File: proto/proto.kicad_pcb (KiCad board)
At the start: 4 copper layers, 57.7 x 90 mm, 17 parts, among them J1 J1, J2 J2, J3 J3, J4 J4, J5 J5, U2 TPIC6595

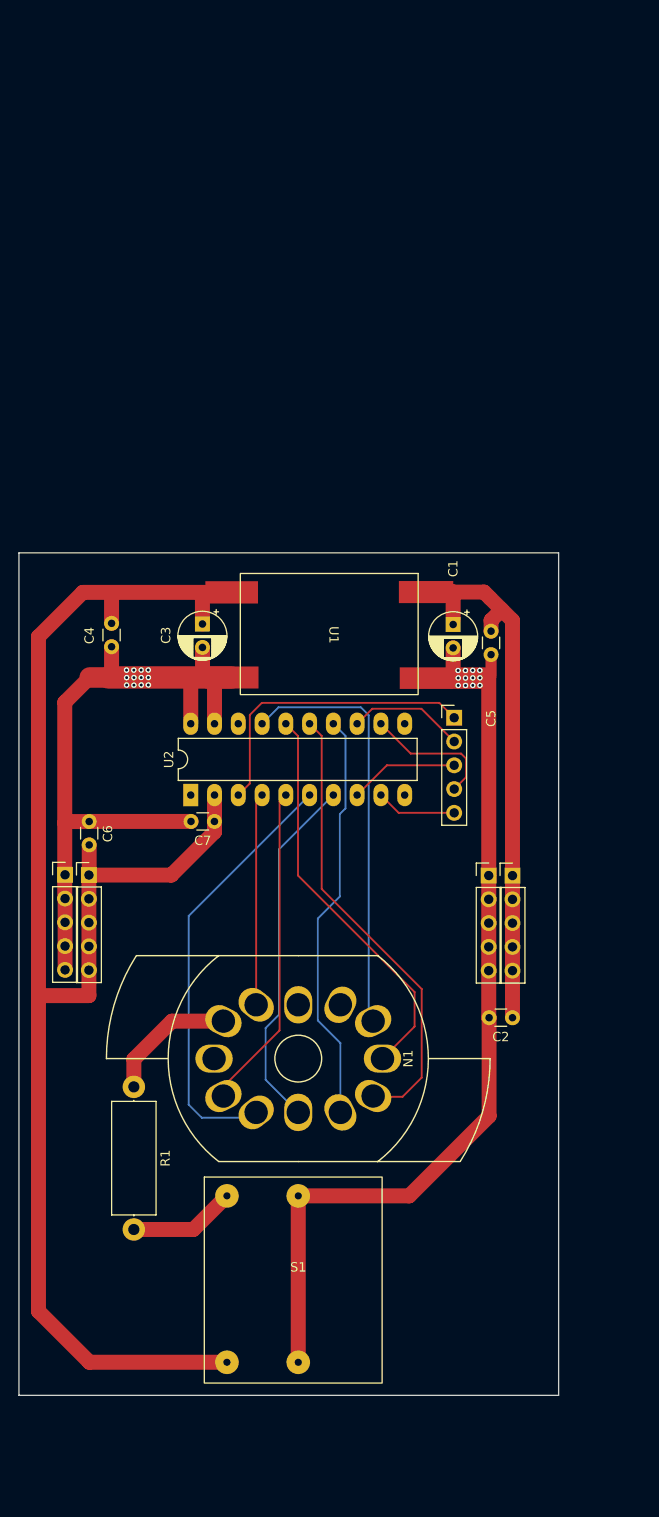
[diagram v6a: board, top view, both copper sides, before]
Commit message: Review and regenerate Gerbers.
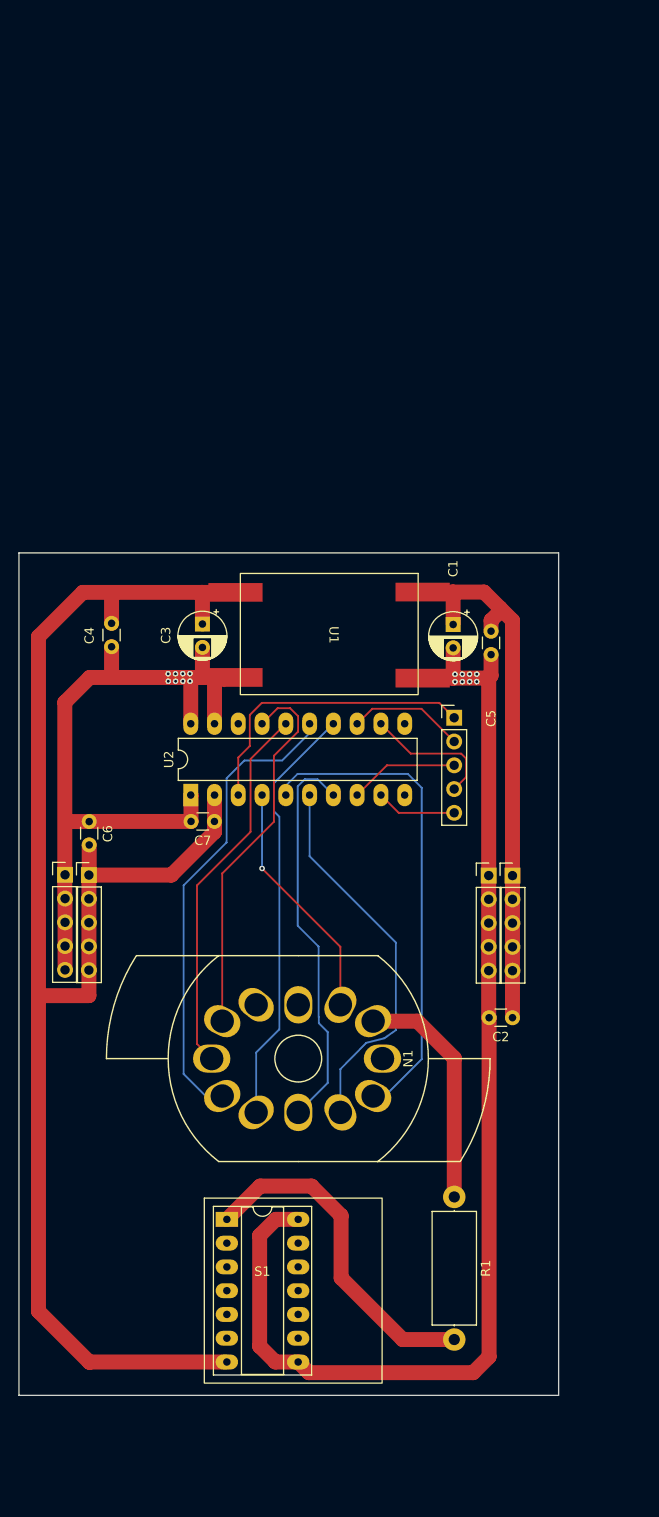
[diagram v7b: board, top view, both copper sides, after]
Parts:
- moved R1 36.2 mm to (126.1, 160.3)
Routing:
- net Net-(S1-HV_OUT): track 11.4 -> 36.5 mm
- net Net-(N1-D1): track 34.9 -> 53.5 mm
- net GND: track 231.1 -> 216.7 mm, vias 24 -> 16
- net Net-(N1-A): track 14.2 -> 25.8 mm
- net Net-(N1-D2): track 46.5 -> 41.0 mm
- net Net-(N1-D7): track 45.4 -> 40.8 mm
- net Net-(N1-D0): track 22.7 -> 27.1 mm, vias 0 -> 1
- net Net-(N1-D3): track 38.4 -> 42.3 mm
- net Net-(J5-Pin_1): track 167.7 -> 164.8 mm
- net Net-(N1-D5): track 48.8 -> 51.5 mm
- net Net-(N1-D6): track 42.9 -> 40.4 mm
- net Net-(J2-Pin_1): track 62.1 -> 59.6 mm
- net Net-(N1-D4): track 44.3 -> 46.2 mm
